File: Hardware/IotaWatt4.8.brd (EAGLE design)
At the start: 87 x 67.9 mm, 53 parts

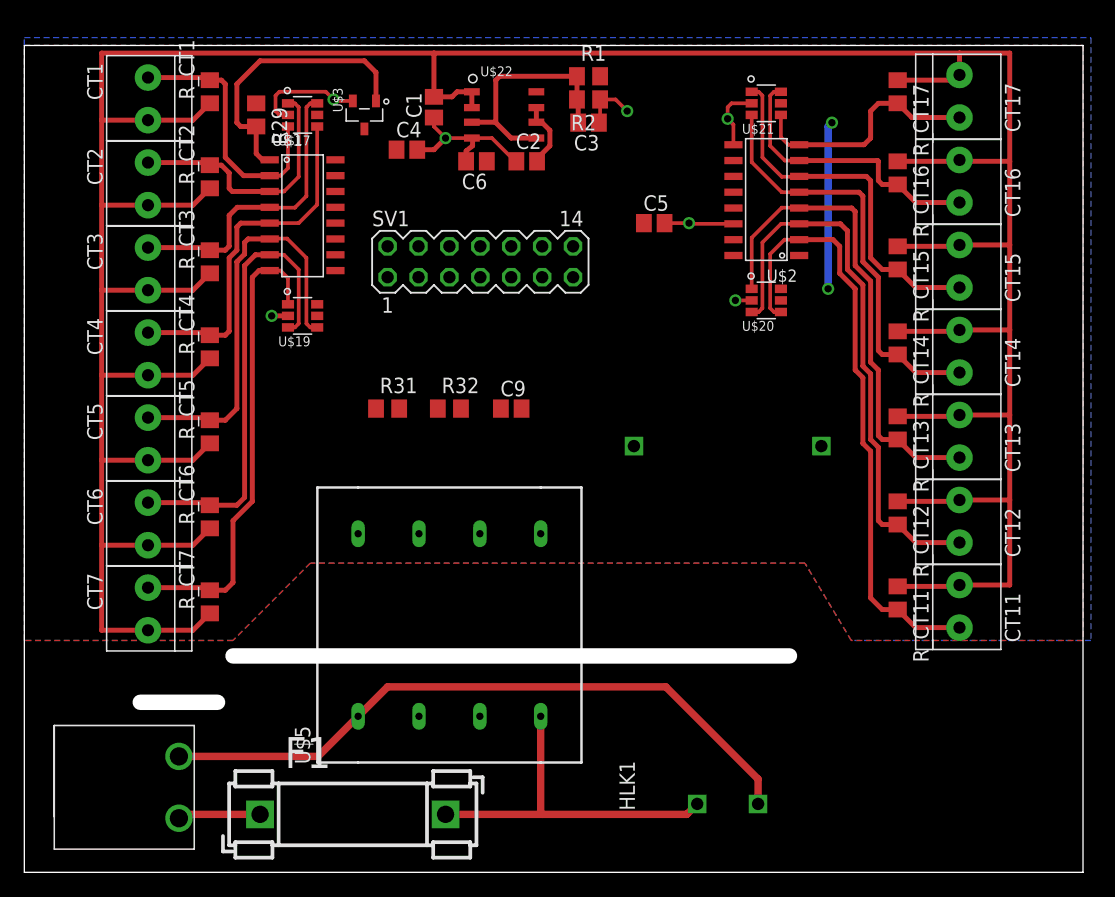
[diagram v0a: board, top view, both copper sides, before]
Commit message: completed routing for both boards
routed out both the base and IO board. Should be ready for verification
There will be errors.
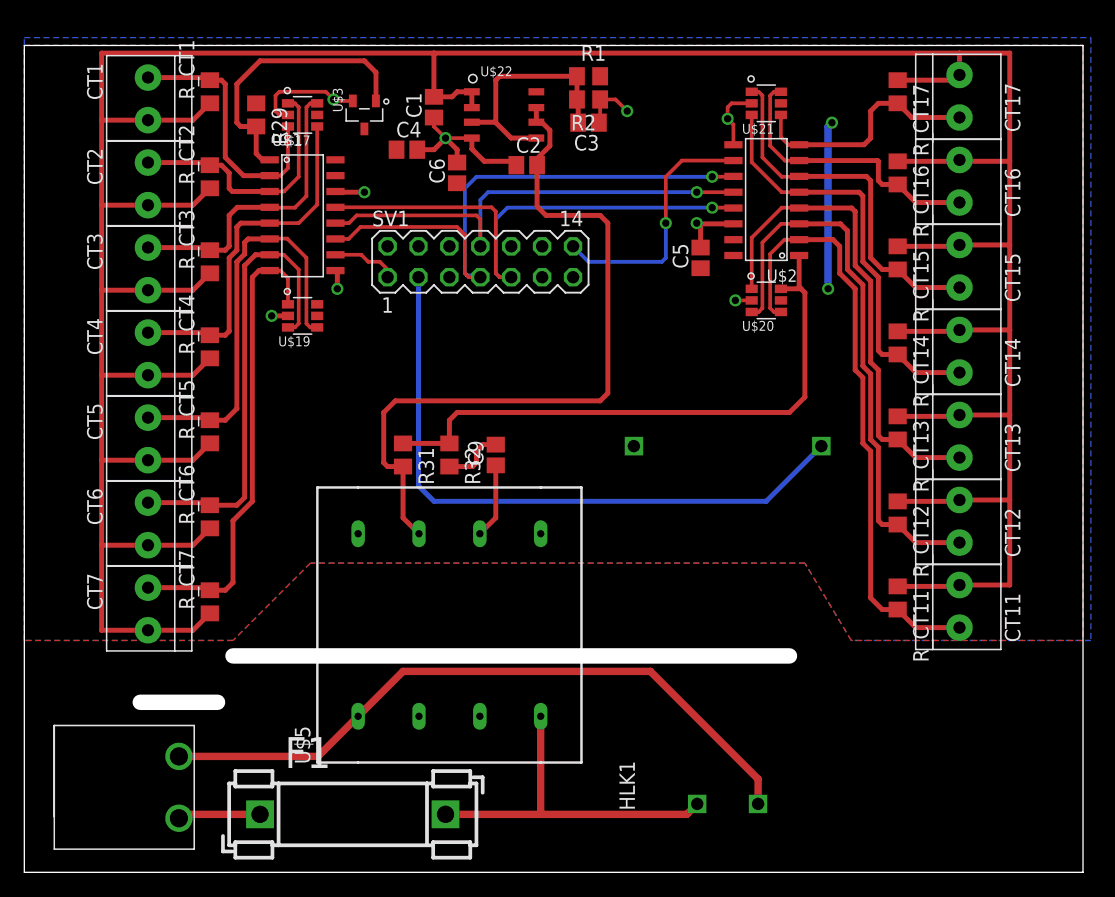
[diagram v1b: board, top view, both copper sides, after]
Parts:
- moved C5 4.76 mm to (56.2, 50.5), turned to 90 degrees
- moved C9 4.02 mm to (39.4, 34.3), turned to 90 degrees
- moved R31 4.02 mm to (31.8, 34.3), turned to 270 degrees
- moved R32 3.81 mm to (35.6, 34.3), turned to 270 degrees
- moved C6 1.85 mm to (36.2, 57.5), turned to 90 degrees
- moved C2 0.32 mm to (41.9, 58.1)
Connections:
- removed net CSSD: SV1.10
- net 5V: now also SV1.3
- net ADC10: no longer SV1.2
- net ADCCS0: now also SV1.1
- net ADCCS1: now also SV1.14; no longer SV1.3
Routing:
- net ACBIAS: track 5.56 -> 60.6 mm
- net 5V: track 0.00 -> 52.7 mm
- net ADC10: track 0.00 -> 49.2 mm
- net MOSI: track 0.00 -> 46.7 mm, vias 0 -> 1
- net SCLK: track 0.00 -> 45.6 mm, vias 0 -> 1
- net MISO: track 0.00 -> 39.4 mm, vias 0 -> 1
- net ADCCS1: track 0.00 -> 21.1 mm, vias 0 -> 1
- net N$27: track 0.00 -> 6.16 mm
- net ADCCS0: track 0.00 -> 5.42 mm
- net N$17: track 0.00 -> 5.12 mm
- net GND: track 40.6 -> 45.0 mm, vias 7 -> 9
- net N: track 55.1 -> 56.2 mm

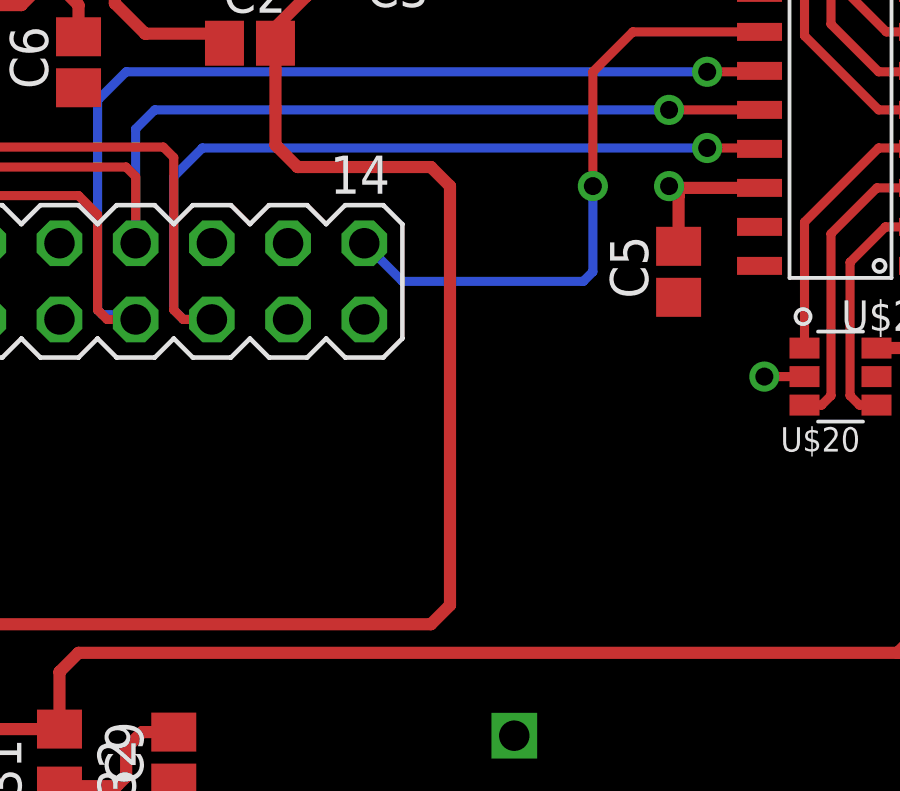
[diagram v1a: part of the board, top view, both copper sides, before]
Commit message: added mechcad files
case and transformer files
case source:
https://eng.italtronic.com/products/modulbox_one_en/4m_modulbox_one_en/
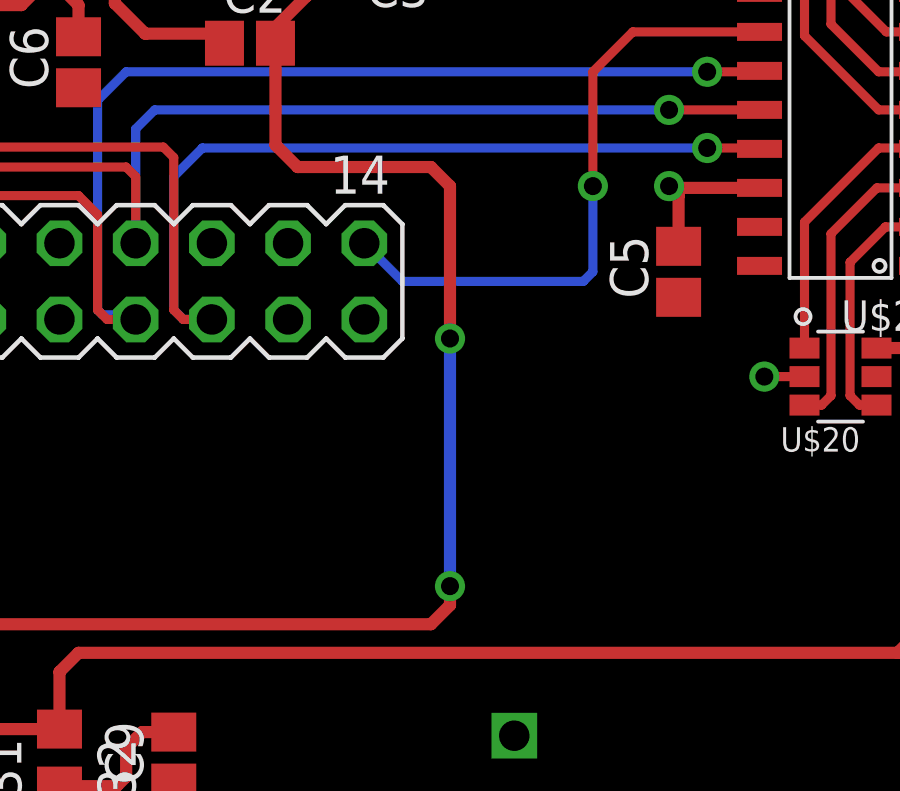
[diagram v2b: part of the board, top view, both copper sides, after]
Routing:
- net ACBIAS: vias 0 -> 2
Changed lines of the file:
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@@
 <wire x1="31.115" y1="38.735" x2="47.9425" y2="38.735" width="0.4064" layer="1"/>
 <wire x1="47.9425" y1="38.735" x2="48.5775" y2="39.37" width="0.4064" layer="1"/>
-<wire x1="48.5775" y1="39.37" x2="48.5775" y2="53.34" width="0.4064" layer="1"/>
+<wire x1="48.5775" y1="39.37" x2="48.5775" y2="40.005" width="0.4064" layer="1"/>
+<wire x1="48.5775" y1="48.26" x2="48.5775" y2="53.34" width="0.4064" layer="1"/>
 <wire x1="48.5775" y1="53.34" x2="47.9425" y2="53.975" width="0.4064" layer="1"/>
 <wire x1="47.9425" y1="53.975" x2="43.4975" y2="53.975" width="0.4064" layer="1"/>
 <wire x1="43.4975" y1="53.975" x2="42.76" y2="54.7125" width="0.4064" layer="1"/>
 <wire x1="42.76" y1="54.7125" x2="42.76" y2="58.1025" width="0.4064" layer="1"/>
+<via x="48.5775" y="48.26" extent="1-16" drill="0.6" shape="octagon"/>
+<via x="48.5775" y="40.005" extent="1-16" drill="0.6" shape="octagon"/>
+<wire x1="48.5775" y1="40.005" x2="48.5775" y2="48.26" width="0.4064" layer="16"/>
 </signal>
 <signal name="N$7">
@@
 <wire x1="52.07" y1="16.51" x2="60.92" y2="7.66" width="0.6096" layer="1"/>
 <wire x1="60.92" y1="7.66" x2="60.92" y2="5.62" width="0.6096" layer="1"/>
-<wire x1="31.75" y1="16.51" x2="28.06" y2="12.82" width="0" layer="19" extent="1-1"/>
+<wire x1="24.765" y1="9.525" x2="28.06" y2="12.82" width="0" layer="19" extent="1-1"/>
 </signal>
 <signal name="N$27">

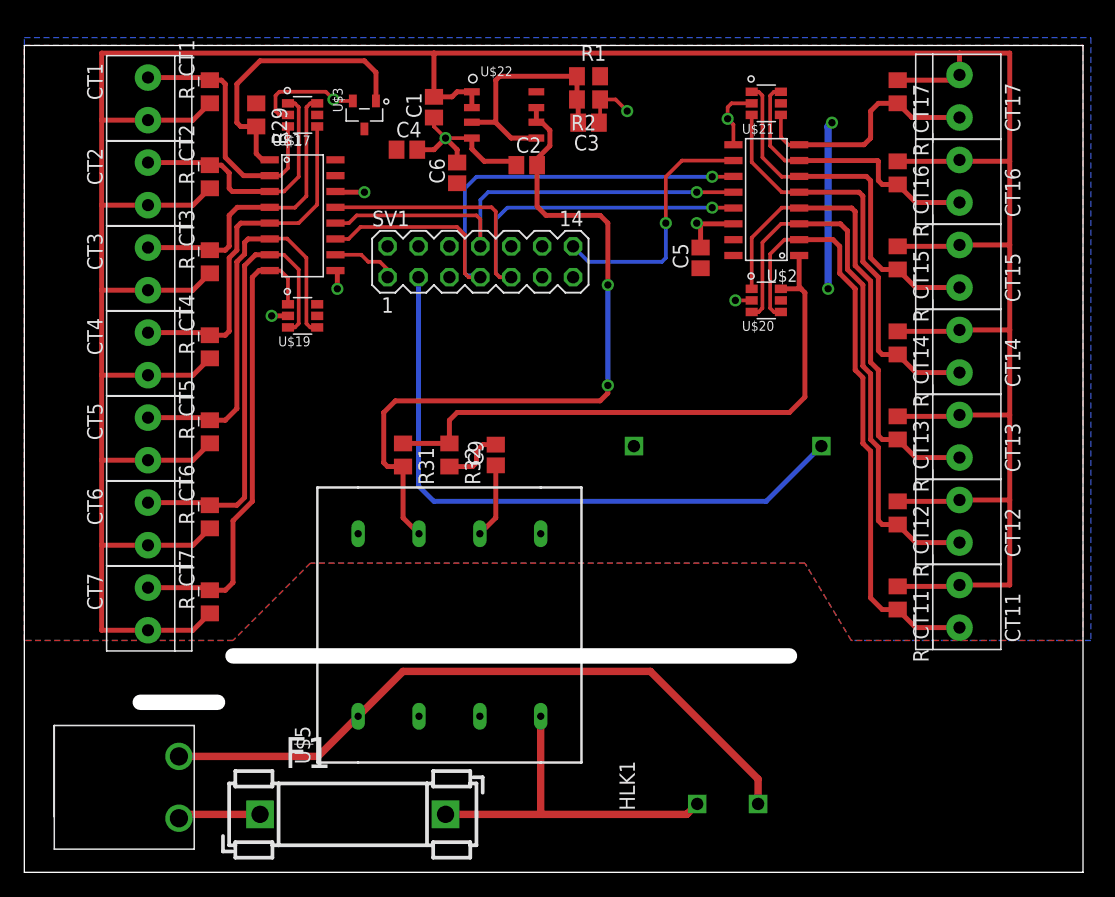
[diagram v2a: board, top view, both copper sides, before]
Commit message: moved the MicroSD
now, there is enough room to remove the card in the enclosure
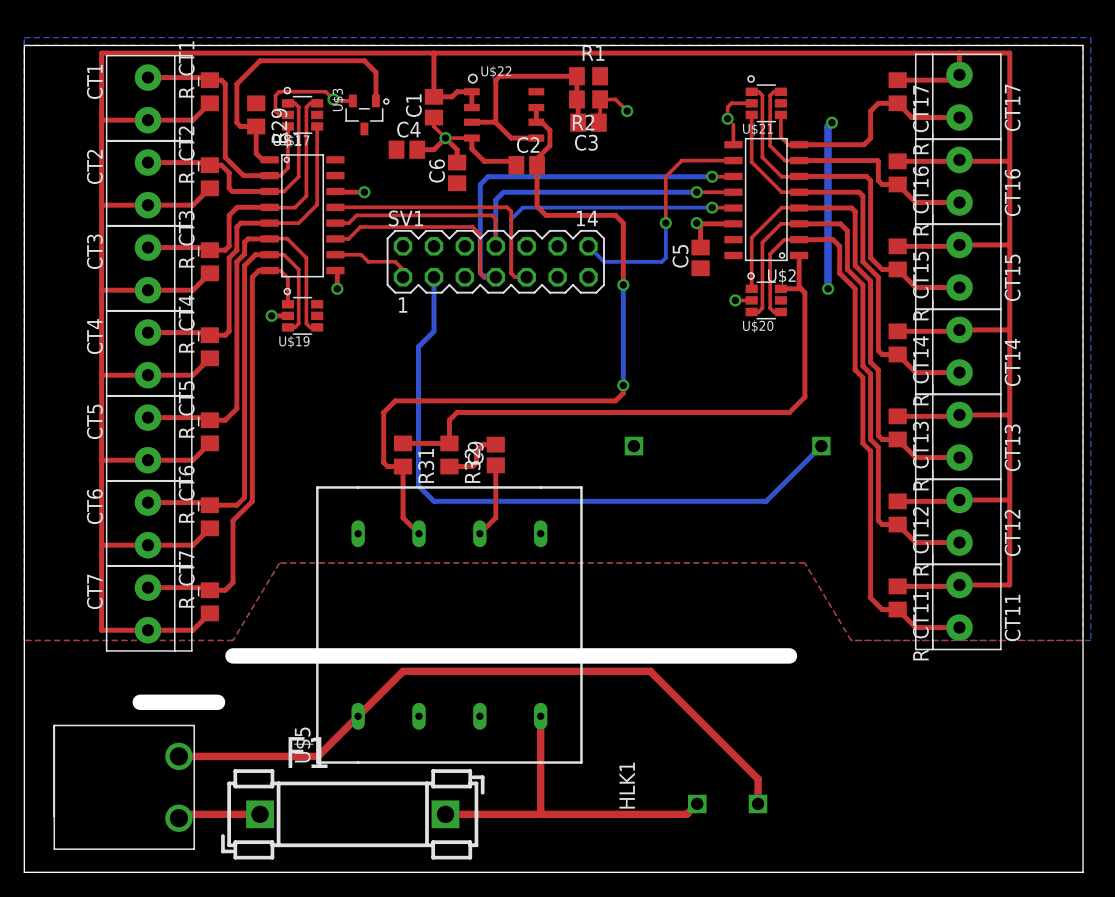
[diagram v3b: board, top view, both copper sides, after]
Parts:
- moved SV1 1.27 mm to (39.4, 50.2)
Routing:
- net ACBIAS: track 60.6 -> 63.1 mm
- net MOSI: track 46.7 -> 48.3 mm
- net ADCCS1: track 21.1 -> 19.8 mm
- net ADCCS0: track 5.42 -> 6.69 mm
- net GND: track 45.0 -> 44.3 mm
- net 5V: track 52.7 -> 53.2 mm

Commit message: fixed some minor errors on the board
fixed some minor errors on the board
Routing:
- net GND: track 44.3 -> 45.0 mm
